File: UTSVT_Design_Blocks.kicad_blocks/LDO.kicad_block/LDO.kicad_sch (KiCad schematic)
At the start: 5 parts, among them U1 MCP1826S

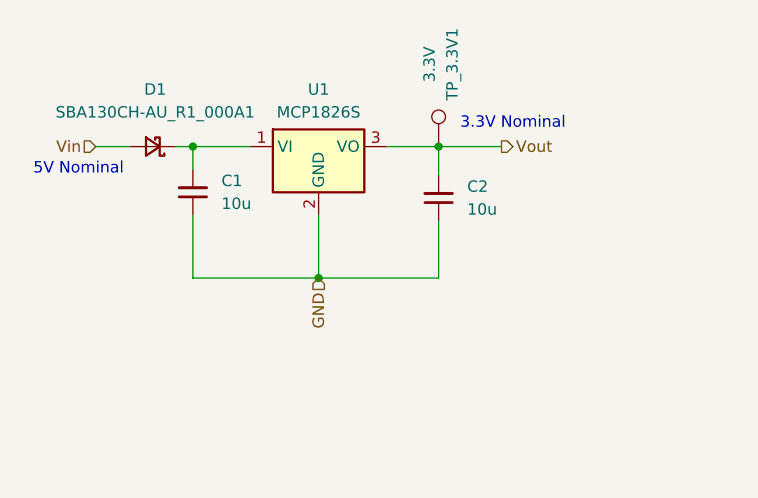
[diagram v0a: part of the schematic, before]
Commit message: replaced symbol with default, replaced footprint with one that matches datasheet exactly
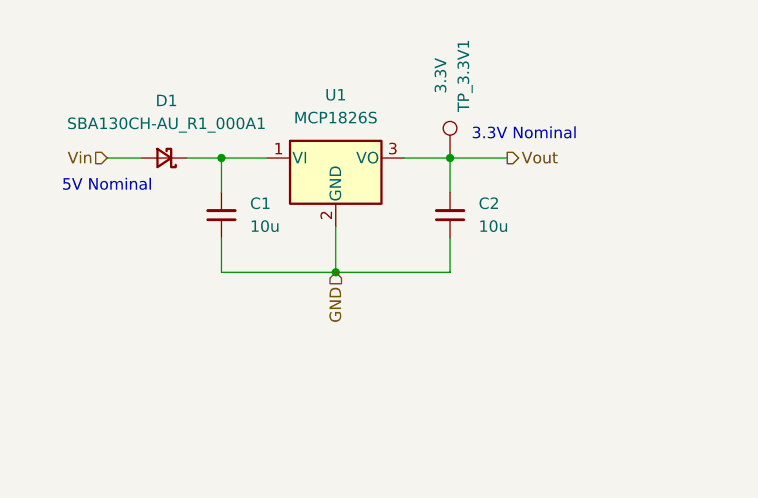
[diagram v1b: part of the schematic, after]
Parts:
- removed U1: MCP1826S, Package_TO_SOT_SMD:SOT-223, symbol LDO_symbol:MCP1826S
- added U1: MCP1826S, Package_TO_SOT_SMD:SOT-223-3_TabPin2, symbol Regulator_Linear:MCP1826S
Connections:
- net GND: now also U1.2 (GND)
- net Vout: now also U1.3 (VO)
- net at C1.2, D1.1 (K): now also U1.1 (VI)
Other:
- moved on the sheet: C1, C2, D1, TP_3.3V1

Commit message: there was a whitespace after P/N
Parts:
- U1: P/N (none) -> MCP1826S-3302E/DB; P/N  MCP1826S-3302E/DB -> (none)
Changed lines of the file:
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@@
 			)
 		)
-		(property "P/N " "MCP1826S-3302E/DB"
+		(property "P/N" "MCP1826S-3302E/DB"
 			(at 152.4 63.5 0)
 			(effects
